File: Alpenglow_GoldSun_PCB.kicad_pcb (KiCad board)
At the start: 2 copper layers, 52.4 x 52.4 mm, 10 parts, among them SW1 SW_SPDT

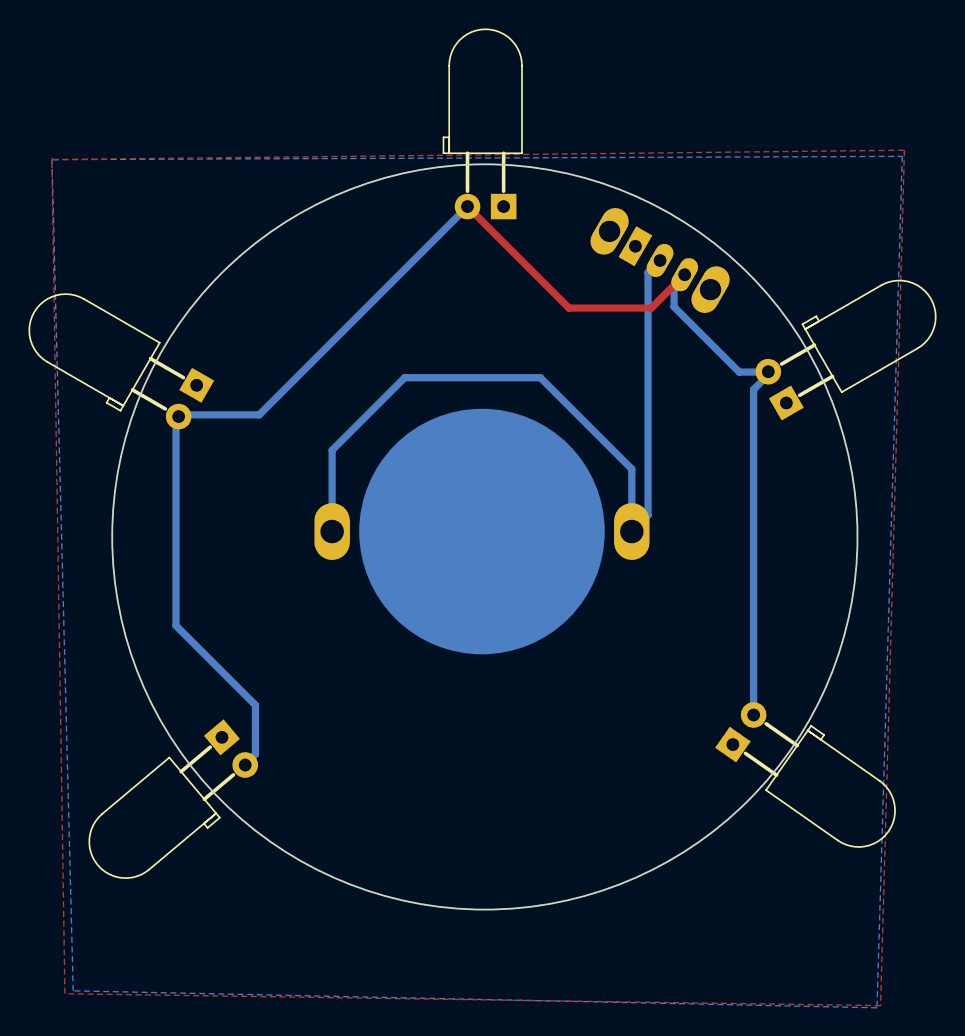
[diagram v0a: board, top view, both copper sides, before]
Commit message: Updated board design with new sun. Ordered prototypes
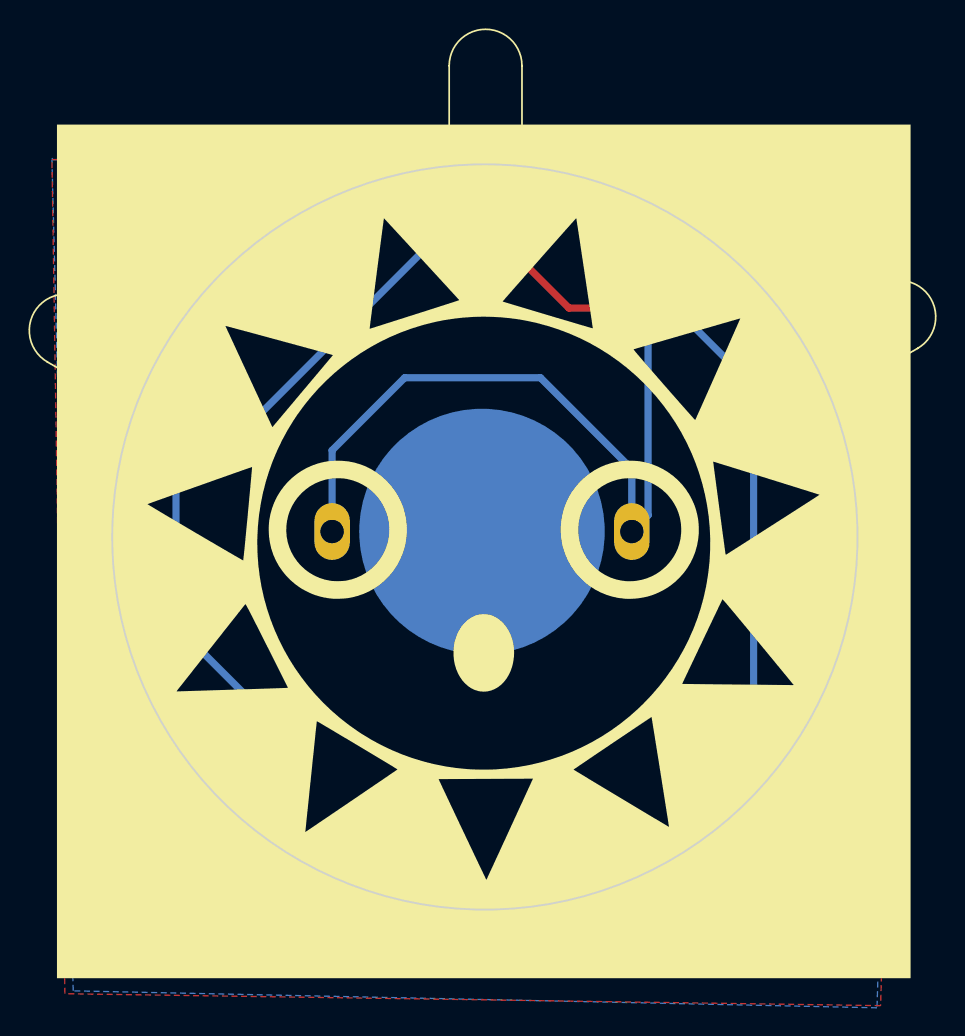
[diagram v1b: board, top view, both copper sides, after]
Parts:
- removed the G*** at (151.8, 91.2)
- added G***: LOGO, Alpenglow_Sun_PCB:Negative Sun 60, F.Cu at (152.5, 90.8)
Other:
- net class Default removed

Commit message: Changed silkscreen so it's a circle instead of a square
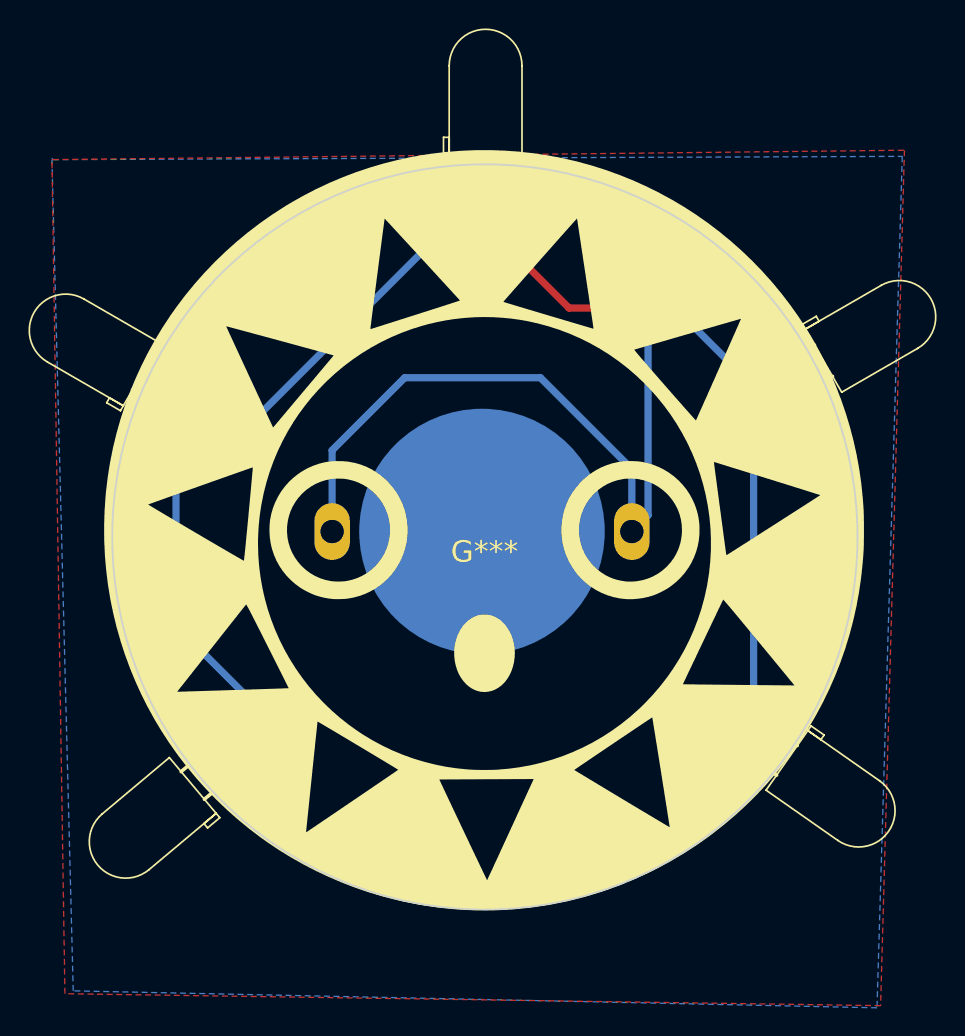
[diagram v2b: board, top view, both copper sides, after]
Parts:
- removed the G*** at (152.5, 90.8)
- added G***: LOGO, Alpenglow_Sun_PCB:Sun Neg for Silk more coverage60mm, F.Cu at (152.6, 90.8)
